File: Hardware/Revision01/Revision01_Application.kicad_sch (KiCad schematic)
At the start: 35 parts, among them J2 Conn_02x08_Odd_Even, J3 Conn_01x04, J4 StrainGaugeMeasurement connec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, Q2 PMV32UP,215, Q3 PMV32UP,215, U2 MRF89XAM9AT-I/RM, U4 ICM-45605

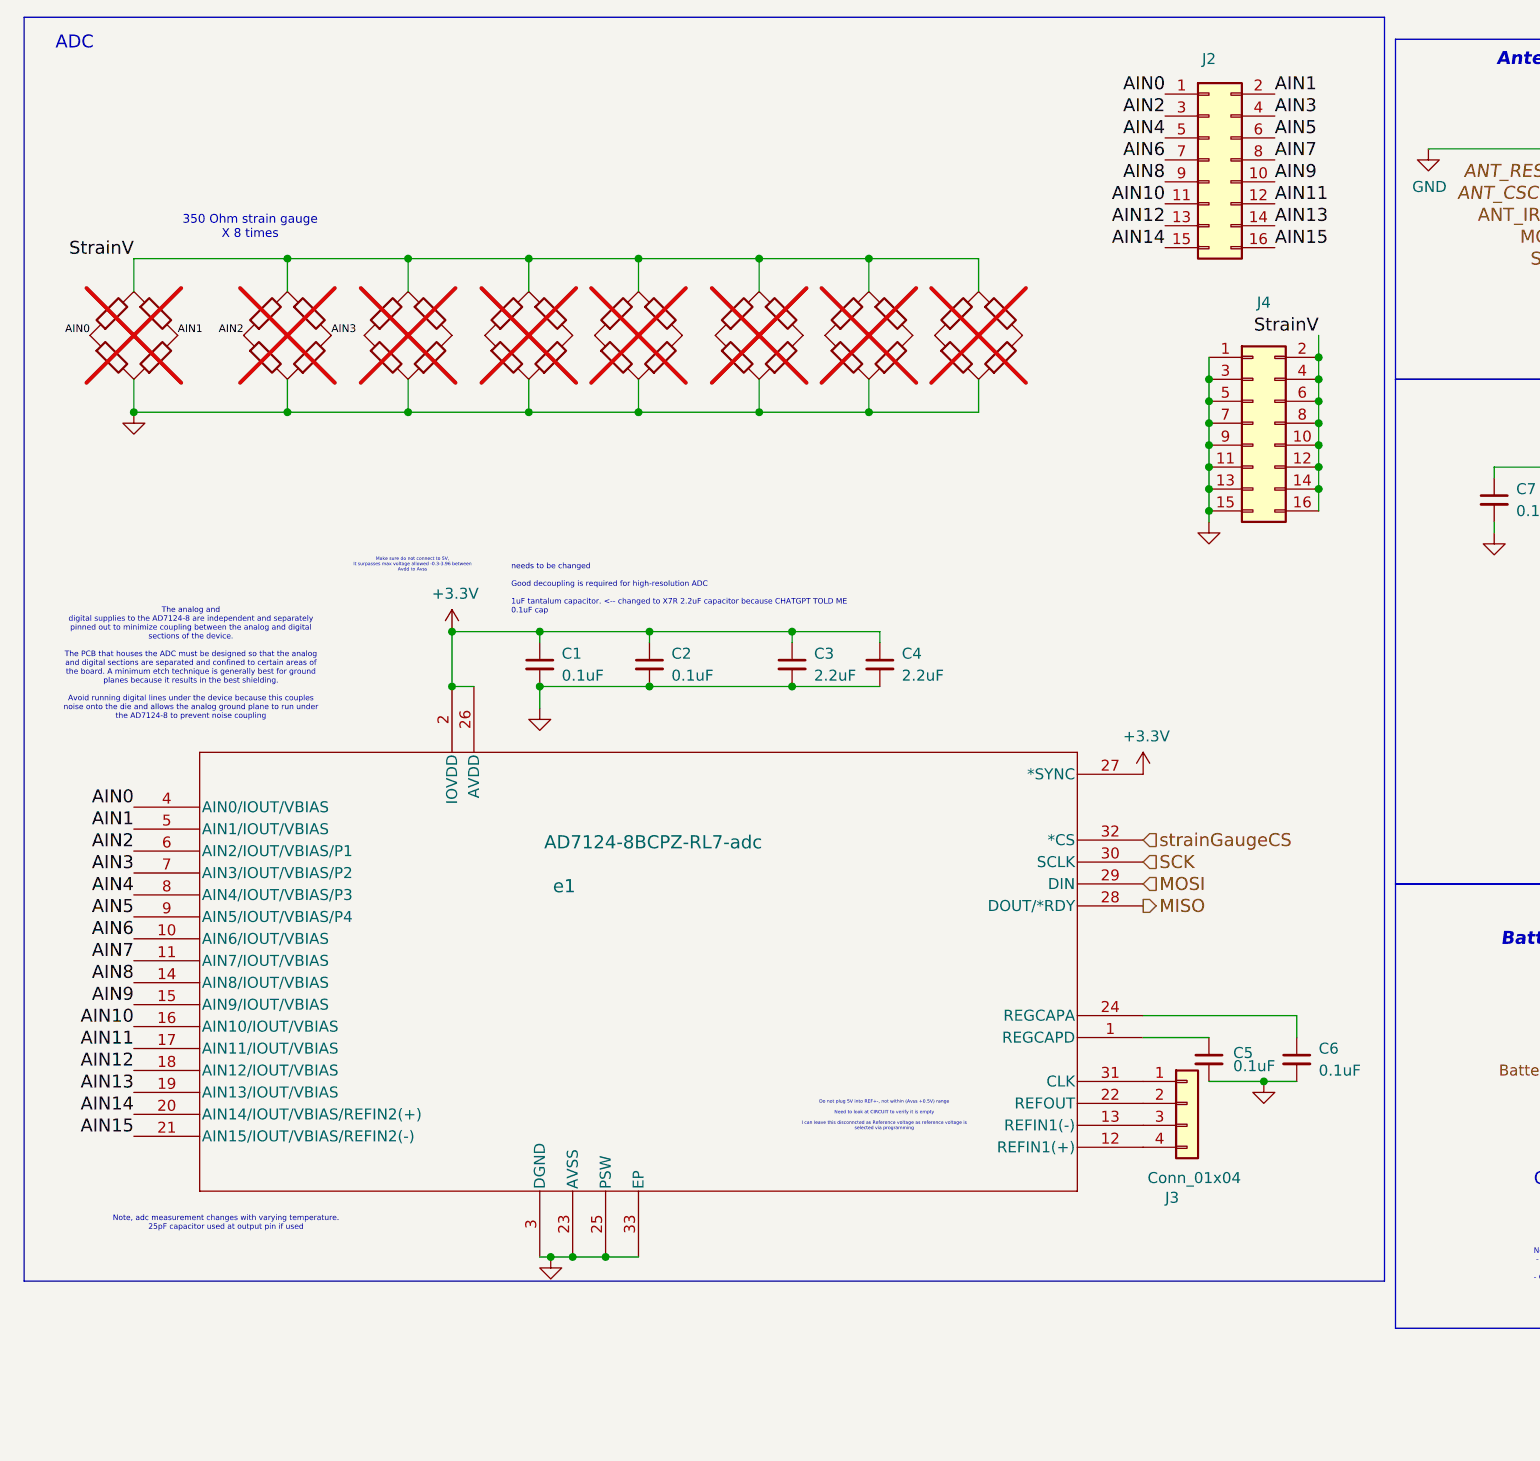
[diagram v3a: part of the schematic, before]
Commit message: added connection for ADC PSW
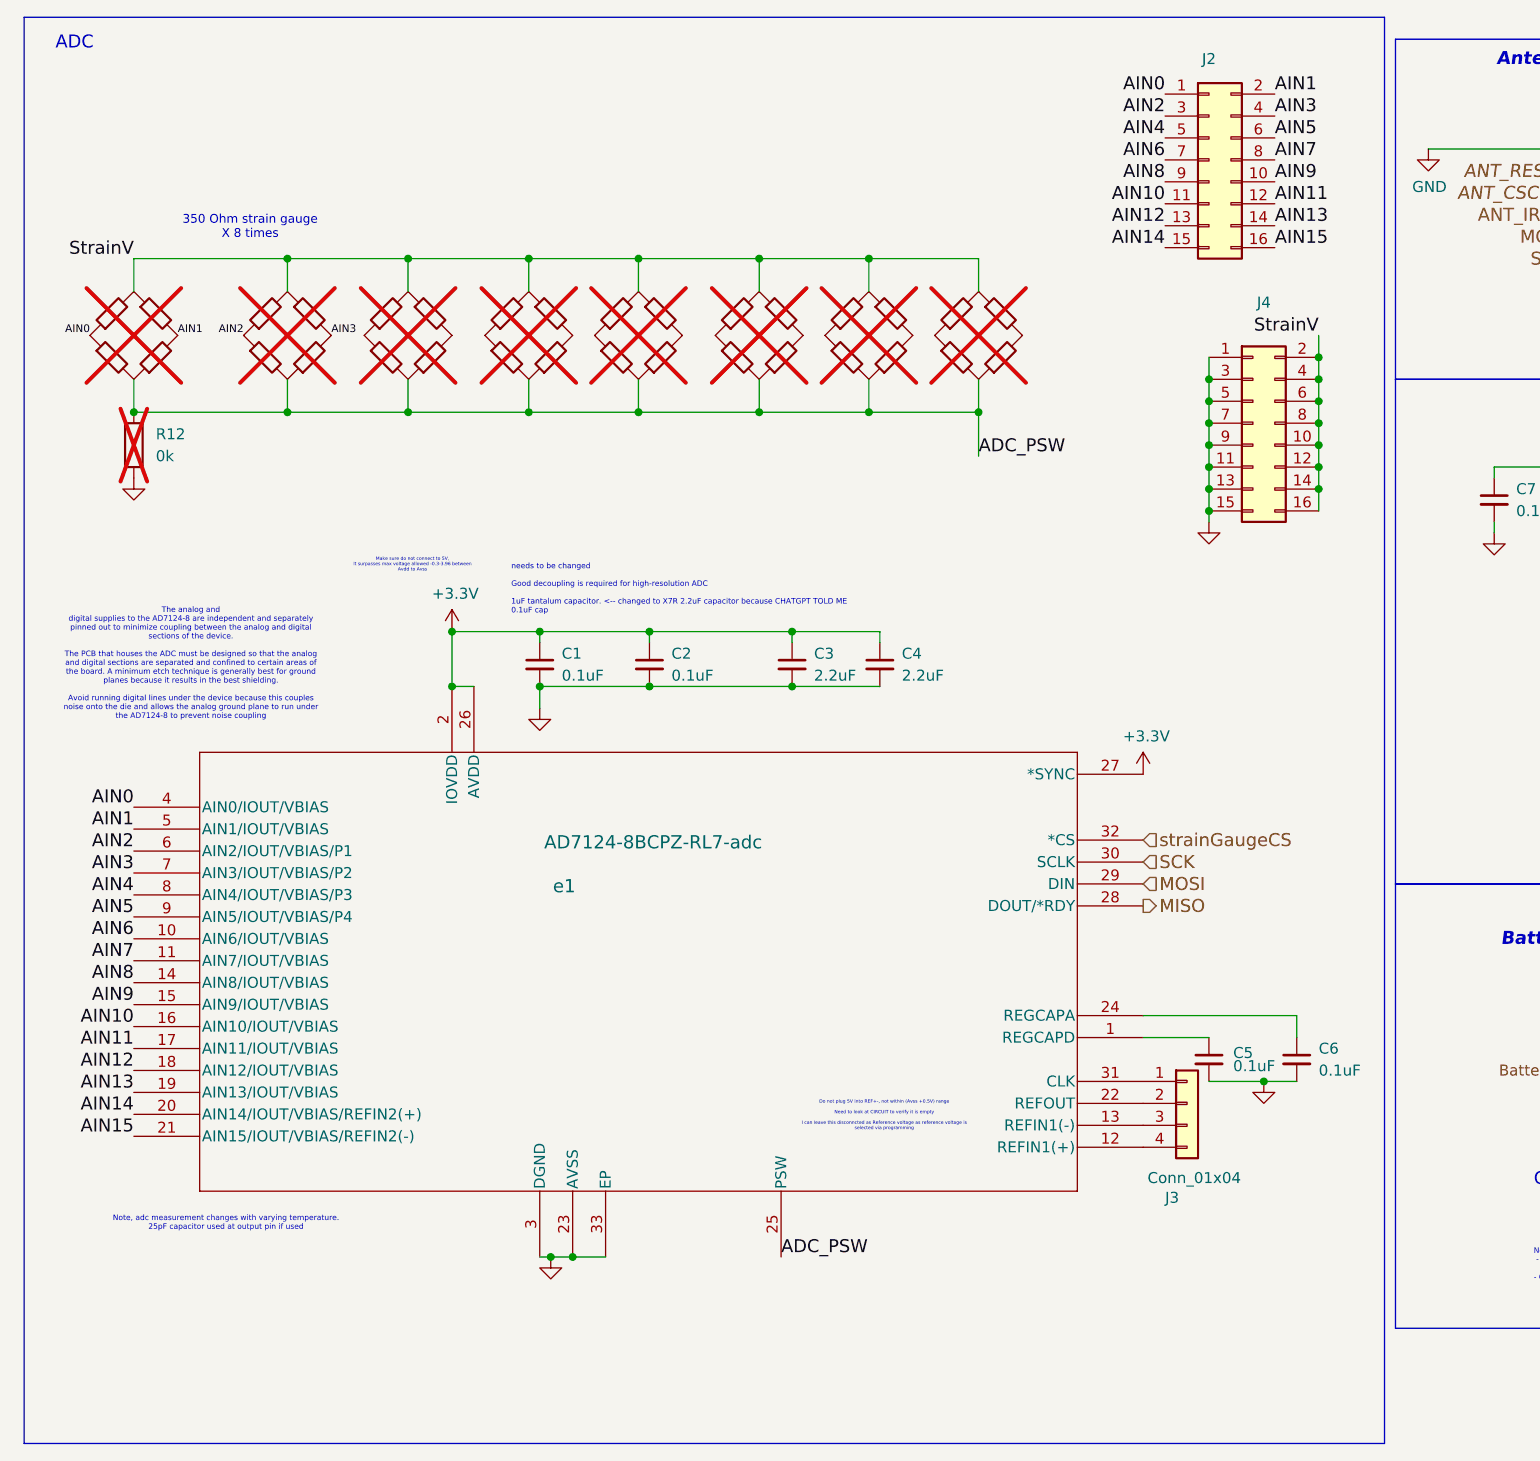
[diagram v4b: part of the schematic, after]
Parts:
- added R12: 0k, symbol Device:R
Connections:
- net GND: now also R12.1; no longer R18.1, R3.1, R4.1, R5.1, R6.1, R7.1, R8.1, R9.1, e1.25 (PSW)
- new net ADC_PSW: R12.2, R18.1, R3.1, R4.1, R5.1, R6.1, R7.1, R8.1, R9.1, e1.25 (PSW)

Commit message: wired REFIN-, REFIN+ wired internal lowside ADC PS Changed VCC_STRAIN_GAUGE from 5V -> 3.3V to ensure the measured voltages are within 0-3.3V
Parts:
- added R13, R14: 0k, symbol Device:R
- J3: footprint Connector_PinHeader_2.54mm:PinHeader_1x04_P2.54mm_Vertical -> Connector_PinHeader_2.54mm:PinHeader_1x02_P2.54mm_Vertical; symbol Connector_Generic:Conn_01x04 -> Connector_Generic:Conn_01x02
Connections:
- net +3.3V: now also e1.12 (REFIN1(+)), R14.2
- net +5V: now also R13.2
- net ADC_PSW: now also e1.13 (REFIN1(-))
- net StrainV: no longer R18.1, R3.1, R4.1, R5.1, R6.1, R7.1, R8.1, R9.1
- new net: R13.1, R14.1, R18.1, R3.1, R4.1, R5.1, R6.1, R7.1, R8.1, R9.1
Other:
- note added: "Bridge Power Switch (PSW) A low-side power switch allows the user to power down bridges that are interfaced to the ADC."
- note added: "Strain Gauge Pwr enable - SOON TO BE REMOVED"
- note added: "What exactly is Reference voltage referring to. The device contains a 2.5 V reference, which has a drift of 15 ppm/°C maximum for the AD7124-8 and AD7124-8 W grade and 10 ppm/°C maximum for the AD7124-8 B grade. Reference buffers are also included on chip, which can be used with the internal reference and externally applied references."
- note removed: "Strain Gauge Pwr enable"
- moved on the sheet: C11, J2, J4, Q2, R10, R11, R12, TP14, TP15

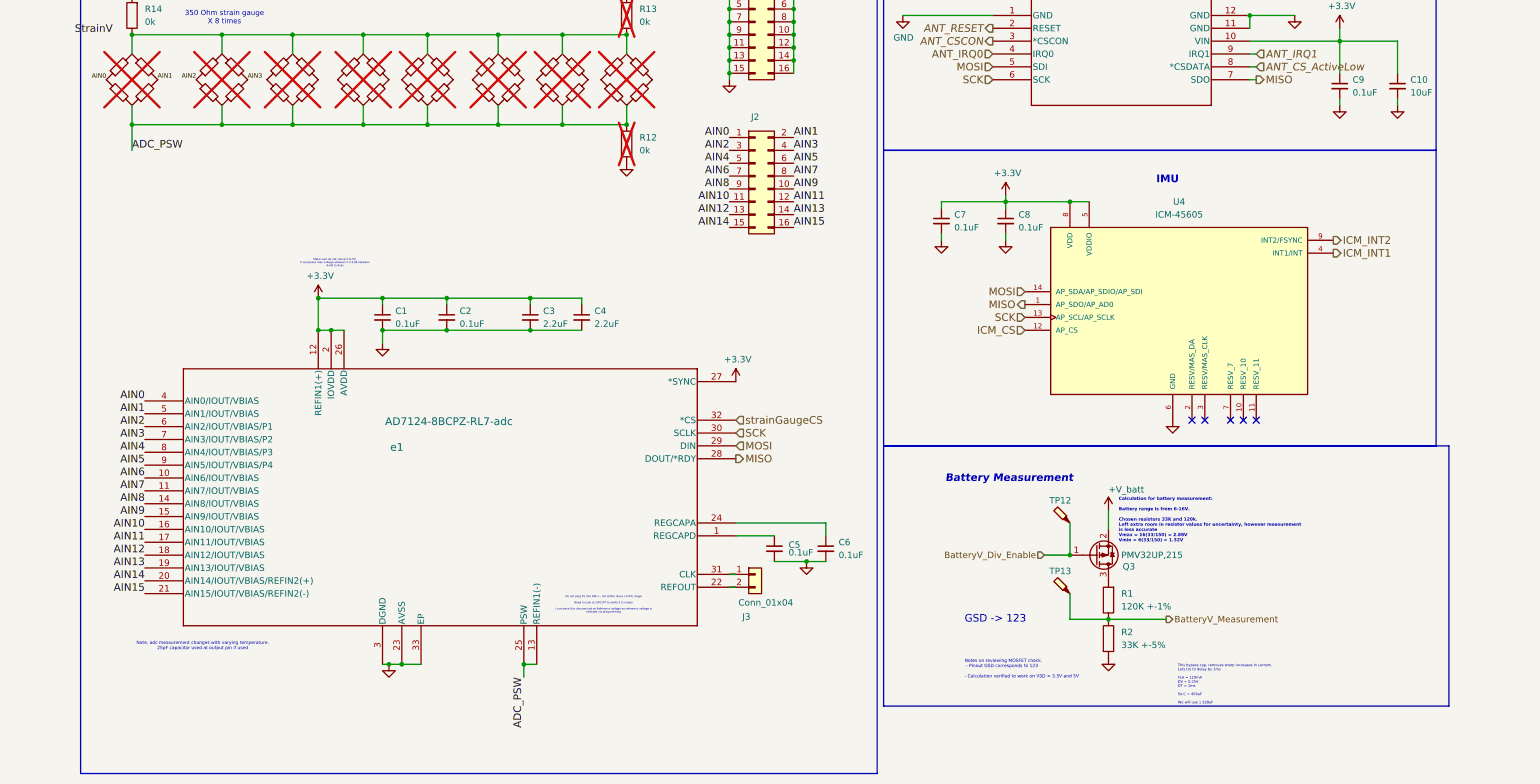
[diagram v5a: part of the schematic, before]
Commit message: Stimulated new battery measurement circuit(Which uses a load switch)
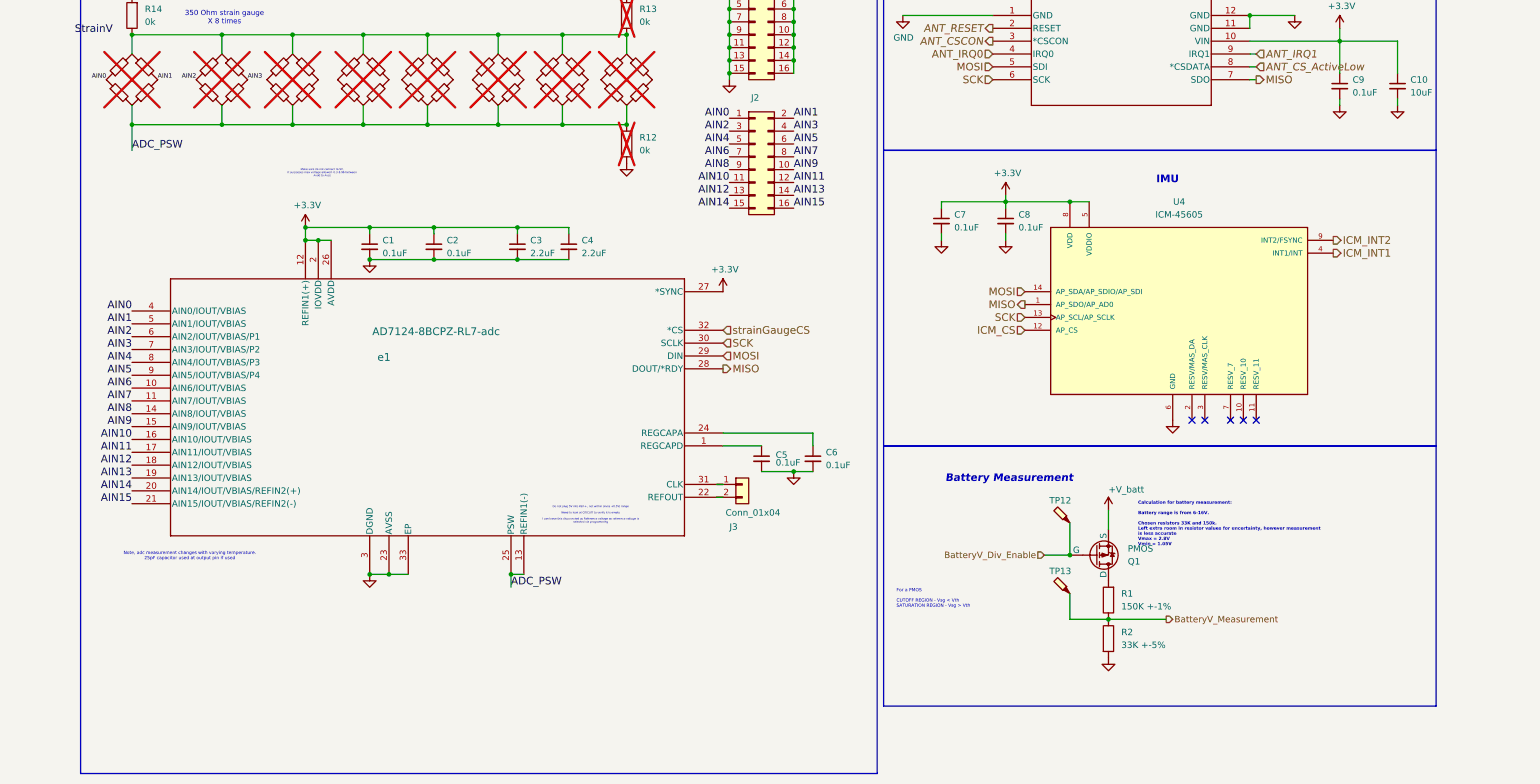
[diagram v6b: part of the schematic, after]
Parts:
- removed Q3: PMV32UP,215, Package_TO_SOT_SMD:SOT-23, symbol Transistor_FET:Q_PMOS_GSD
- added Q1: PMOS, symbol Simulation_SPICE:PMOS
- R1: value 120K +-1% -> 150K +-1%; Distributor link https://www.digikey.ca/en/products/detail/koa-speer-electro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 -> (none); Manufacturer Part Number RK73H2ATTD1203F -> (none)
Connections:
- net +V_batt: now also Q1.3 (S)
- net BatteryV_Div_Enable: now also Q1.2 (G)
- net at R1.2: now also Q1.1 (D)
- new net: R13.1, R14.1, R18.1, R3.1, R4.1, R5.1, R6.1, R7.1, R8.1, R9.1
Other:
- note added: "Calculation for battery measurement: Battery range is from 6-16V. Chosen resistors 33K and 150k. Left extra room in resistor values for uncertainty, however measurement is less accurate Vmax = 2.8V Vmin = 1.05V"
- note added: "For a PMOS CUTOFF REGION - Vsg < Vth SATURATION REGION - Vsg > Vth"
- note removed: "Calculation for battery measurement: Battery range is from 6-16V. Chosen resistors 33K and 120k. Left extra room in resistor values for uncertainty, however measurement is less accurate Vmax = 16(33/150) = 2.88V Vmin = 6(33/150) = 1.32V"
- note removed: "GSD -> 123"
- note removed: "Notes on reviewing MOSFET check. - Pinout GSD corresponds to 123 - Calculation verified to work on VSD = 3.3V and 5V"
- note removed: "This bypass cap, removes sharp increases in current. Lets try to delay by 1ms FLA = 110mA DV = 0.25V DT = 1ms So C = 456uF We will use 1 220uF"
- moved on the sheet: C1, C2, C3, C4, C5, C6, J2, J3, e1

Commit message: added new battery measurement circuit which uses load switches onto schematic and changed headers to screw terminals
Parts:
- removed J2: Conn_02x08_Odd_Even, Connector_PinHeader_2.54mm:PinHeader_2x08_P2.54mm_Vertical, symbol Connector_Generic:Conn_02x08_Odd_Even
- removed J4: StrainGaugeMeasurement connector, Connector_PinHeader_2.54mm:PinHeader_2x08_P2.54mm_Vertical, symbol Connector_Generic:Conn_02x08_Odd_Even
- removed Q1: PMOS, symbol Simulation_SPICE:PMOS
- removed R2: 33K +-5%, Resistor_SMD:R_0805_2012Metric, symbol Device:R
- removed TP12, TP13: VBattery_Div_Enable, TestPoint:TestPoint_Pad_D1.5mm, symbol Connector:TestPoint_Probe
- added C12: 0.1uF, Capacitor_SMD:C_0805_2012Metric, symbol Device:C_Small
- added J2: StrainVCC, symbol Connector:Screw_Terminal_01x08
- added J5: Differential Inputs, symbol Connector:Screw_Terminal_01x16
- added J6: StrainGND, symbol Connector:Screw_Terminal_01x08
- added Q3: NMOS, Package_TO_SOT_SMD:TSOT-23, symbol Simulation_SPICE:NMOS
- added Q4: PMOS, Package_TO_SOT_SMD:TSOT-23, symbol Simulation_SPICE:PMOS
- added R16, R17: 10K +-5%, Resistor_SMD:R_0805_2012Metric, symbol Device:R
- added R19: 3.3K +-1%, Resistor_SMD:R_0805_2012Metric, symbol Device:R
- added TP7, TP8: TestPoint, TestPoint:TestPoint_THTPad_1.0x1.0mm_Drill0.5mm, symbol Connector:TestPoint
- C10: Manufacturer Part Number KGM21NR71E104KT -> CL31B106KAHNNNE
- C3, C4: value 2.2uF -> 1uF; footprint Capacitor_SMD:C_0603_1608Metric -> Capacitor_SMD:C_0805_2012Metric; Distributor link https://www.digikey.ca/en/products/detail/samsung-electro-m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 -> https://www.digikey.ca/en/products/detail/vishay-sprague/TL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; MPN CL05B104KP5NNNC -> (none); Manufacturer Part Number CL31B106KAHNNNE -> TL8W9105M016C; URL https://www.digikey.ca/en/products/detail/samsung-electro-m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 -> (none)
- R1: value 150K +-1% -> 15K +-1%; Distributor link (none) -> https://www.digikey.ca/en/products/detail/te-connectivity-p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; Manufacturer Part Number (none) -> CRG0805F15K
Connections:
- net +V_batt: now also Q4.3 (S), R16.2, TP8.1
- net ADC_PSW: now also R18.3, R3.3, R4.3, R5.3, R6.3, R7.3, R8.3, R9.3, J6.1 (Pin_1), J6.2 (Pin_2), J6.3 (Pin_3), J6.4 (Pin_4), J6.5 (Pin_5), J6.6 (Pin_6), J6.7 (Pin_7), J6.8 (Pin_8); no longer R18.1, R3.1, R4.1, R5.1, R6.1, R7.1, R8.1, R9.1
- net AIN0: now also R3.4, J5.1 (Pin_1); no longer R3.1
- net AIN1: now also J5.2 (Pin_2)
- net AIN10: now also J5.11 (Pin_11)
- net AIN11: now also J5.12 (Pin_12)
- net AIN12: now also J5.13 (Pin_13)
- net AIN13: now also J5.14 (Pin_14)
- net AIN14: now also J5.15 (Pin_15)
- net AIN15: now also J5.16 (Pin_16)
- net AIN2: now also R4.4, J5.3 (Pin_3); no longer R4.1
- net AIN3: now also J5.4 (Pin_4)
- net AIN4: now also J5.5 (Pin_5)
- net AIN5: now also J5.6 (Pin_6)
- net AIN6: now also J5.7 (Pin_7)
- net AIN7: now also J5.8 (Pin_8)
- net AIN8: now also J5.9 (Pin_9)
- net AIN9: now also J5.10 (Pin_10)
- net BatteryV_Div_Enable: now also Q3.2 (G), R17.2
- net BatteryV_Measurement: now also C12.1, R19.2, TP7.1
- net GND: now also C12.2, Q3.3 (S), R17.1, R19.1
- net StrainV: now also R13.1, R14.1, R18.1, R3.1, R4.1, R5.1, R6.1, R7.1, R8.1, R9.1, J2.1 (Pin_1), J2.2 (Pin_2), J2.3 (Pin_3), J2.4 (Pin_4), J2.5 (Pin_5), J2.6 (Pin_6), J2.7 (Pin_7), J2.8 (Pin_8)
- net at R1.2: now also Q4.1 (D)
- new net: Q3.1 (D), Q4.2 (G), R16.1
- no-connect marks 5 -> 17
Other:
- note removed: "Bridge Power Switch (PSW) A low-side power switch allows the user to power down bridges that are interfaced to the ADC."
- note removed: "The analog and digital supplies to the AD7124-8 are independent and separately pinned out to minimize coupling between the analog and digital sections of the device. The PCB that houses the ADC must be designed so that the analog and digital sections are separated and confined to certain areas of the board. A minimum etch technique is generally best for ground planes because it results in the bes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"
- note removed: "What exactly is Reference voltage referring to. The device contains a 2.5 V reference, which has a drift of 15 ppm/°C maximum for the AD7124-8 and AD7124-8 W grade and 10 ppm/°C maximum for the AD7124-8 B grade. Reference buffers are also included on chip, which can be used with the internal reference and externally applied references."
- note removed: "needs to be changed Good decoupling is required for high-resolution ADC 1uF tantalum capacitor. <-- changed to X7R 2.2uF capacitor because CHATGPT TOLD ME 0.1uF cap"
- moved on the sheet: C10, C7, C8, C9, R1, U2, U4
